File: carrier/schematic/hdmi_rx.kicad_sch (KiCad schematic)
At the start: 8 parts, among them J9001 HDMI-019S, U9001 M24C02-WMN6TP

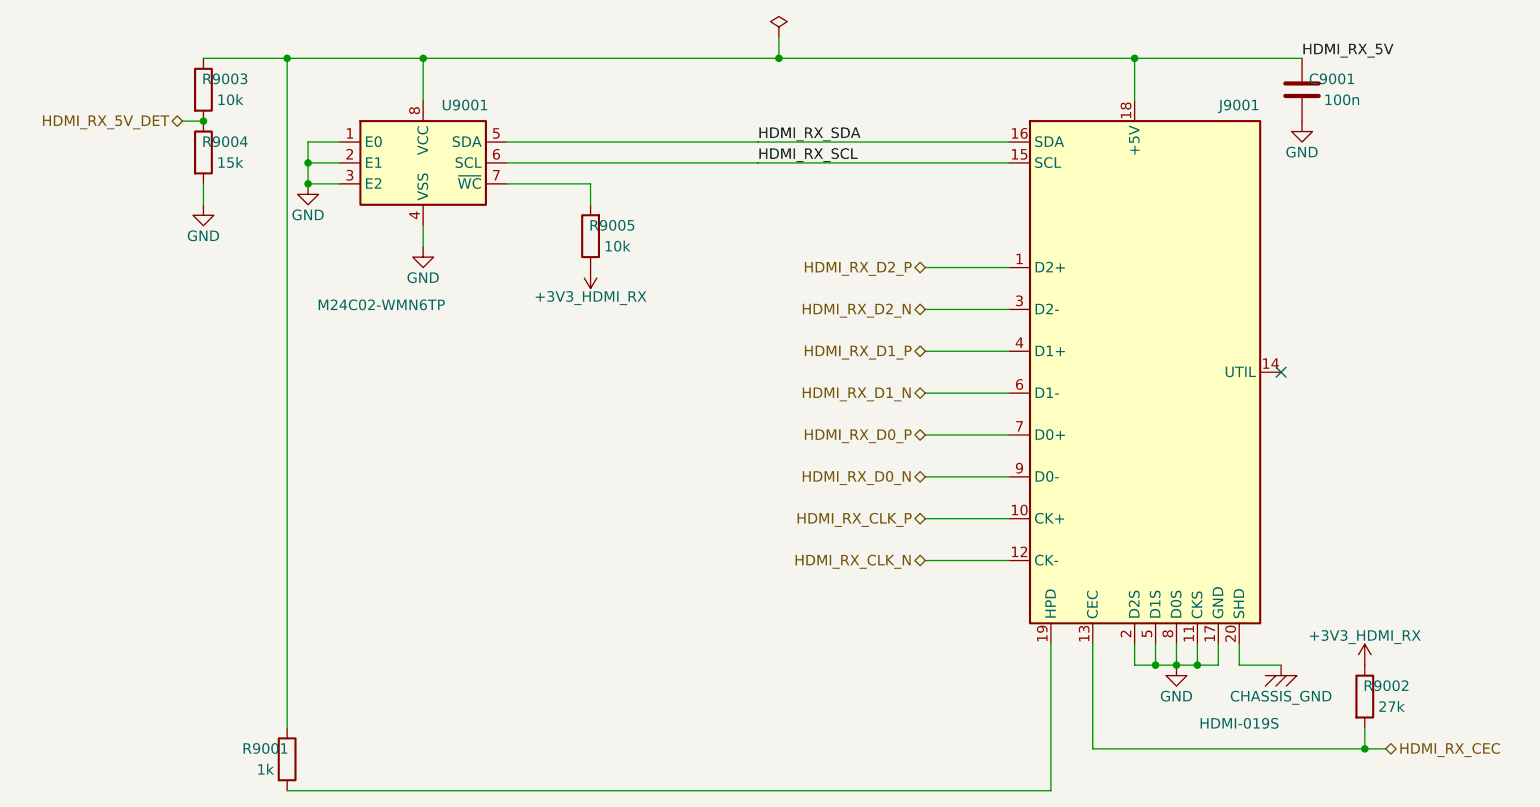
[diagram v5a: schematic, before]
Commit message: hdmi_rx COMP-1: EDID WC# hardwired to its 5V VCC (netlist FIX) + generic place.py escape-lane BFS
COMP-1 closed properly: WC# (U1.7) now on HDMI_RX_5V (the EEPROM's own VCC,
adjacent U1.8) = permanent write-protect at the right rail + above VIH whenever
the EEPROM is powered (carrier on OR off); R5 strap + HDMI_RX_EDID_WP jumper net
deleted. KiCad-extracted netlist confirms /HDMI_RX_5V = {C1,J1.18,R1,R3,U1.7,U1.8}.
The dense-sheet placement that blocked it is solved GENERICALLY in schgen/place.py:
_escape_lane tries both flanks, and direct trunk side-taps get a corner-minimizing
free-cell BFS detour (_bfs_escape, Dijkstra over (cell,heading), vertex-disjoint vs
foreign geometry — cannot short/cross). No gate softened, no sheet-specific hack.
Full regression GREEN: 25 sheets all gates, LINK 0/0, only hdmi_rx+place.py changed
(no other sheet regressed), selftest 44/44 + determinism, m1_rc PASS, render eyeballed.

Co-Authored-By: Claude Fable 5 <noreply@anthropic.com>
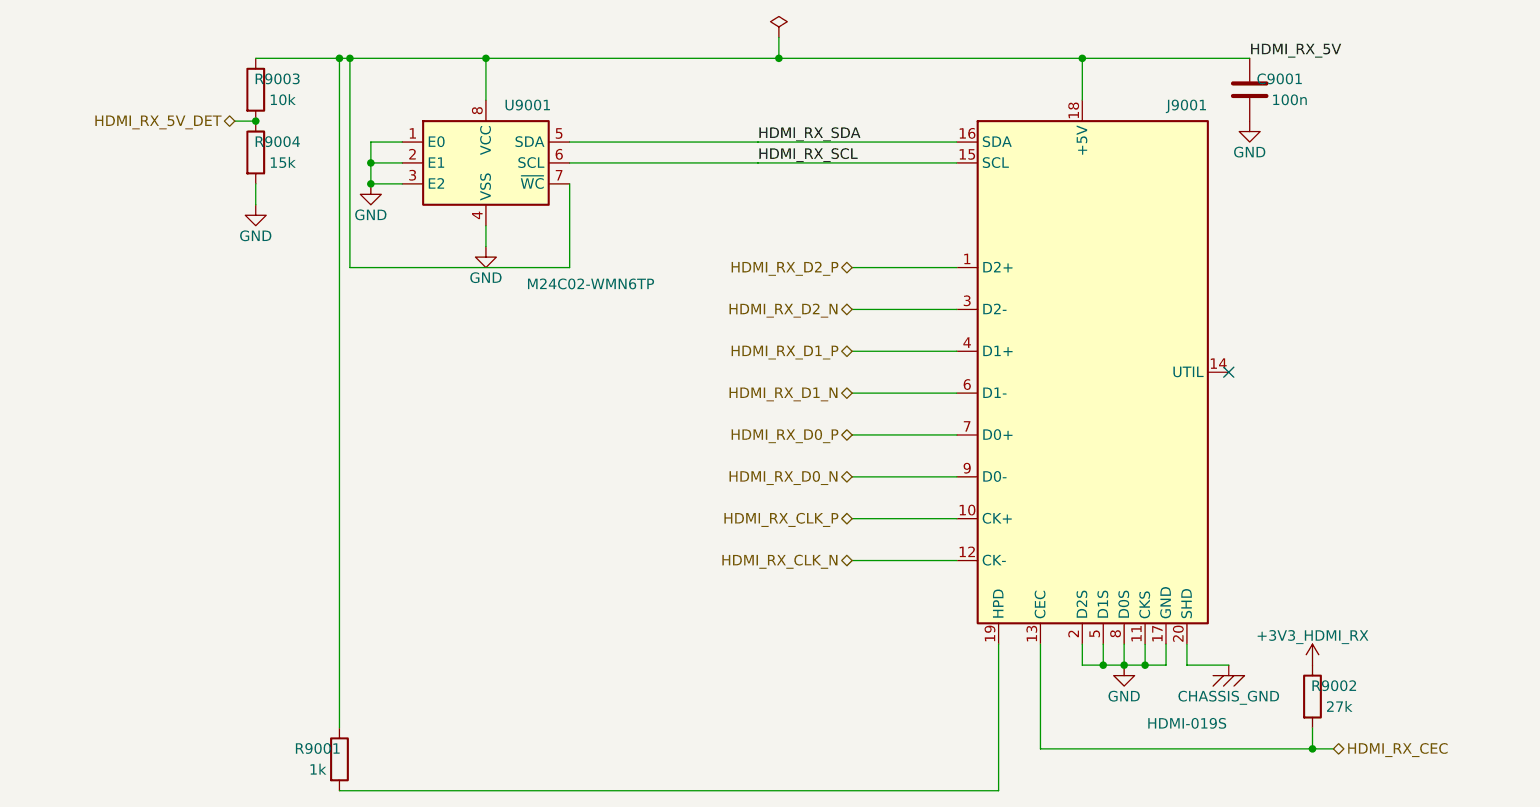
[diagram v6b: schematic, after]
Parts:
- removed C9001: 100n, Capacitor_SMD:C_0603_1608Metric, symbol Device:C
- C9001: renamed from R9004; value 15k -> 100n; footprint Resistor_SMD:R_0603_1608Metric -> Capacitor_SMD:C_0603_1608Metric; symbol Device:R -> Device:C; LCSC C22809 -> C14663
- J9001: renamed from R9005; value 10k -> HDMI-019S; footprint Resistor_SMD:R_0603_1608Metric -> HDMI-019S:HDMI-019S; symbol Device:R -> schgen:HDMI_A_RX; LCSC C25804 -> C111617; MPN (none) -> HDMI-019S
- R9001: renamed from R9002; value 27k -> 1k; LCSC C22967 -> C21190
- R9002: renamed from J9001; value HDMI-019S -> 27k; footprint HDMI-019S:HDMI-019S -> Resistor_SMD:R_0603_1608Metric; symbol schgen:HDMI_A_RX -> Device:R; LCSC C111617 -> C22967; MPN HDMI-019S -> (none)
- R9003: renamed from R9001; value 1k -> 10k; LCSC C21190 -> C25804
- R9004: renamed from R9003; value 10k -> 15k; LCSC C25804 -> C22809
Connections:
- net +3V3_HDMI_RX: now also R9002.1; no longer J9001.1, R9001.1
- net CHASSIS_GND: now also J9001.20 (SHD), J9001.21 (SHD), J9001.22 (SHD), J9001.23 (SHD); no longer R9002.20 (SHD), R9002.21 (SHD), R9002.22 (SHD), R9002.23 (SHD)
- net GND: now also J9001.11 (CKS), J9001.17 (GND), J9001.2 (D2S), J9001.5 (D1S), J9001.8 (D0S), R9004.2; no longer R9002.11 (CKS), R9002.17 (GND), R9002.2 (D2S), R9002.5 (D1S), R9002.8 (D0S)
- net HDMI_RX_5V: now also C9001.1, J9001.18 (+5V), R9001.1, U9001.7 (~{WC}); no longer R9002.18 (+5V), R9004.1
- net HDMI_RX_5V_DET: now also R9003.2, R9004.1; no longer C9001.1, R9004.2
- net HDMI_RX_CEC: now also J9001.13 (CEC), R9002.2; no longer R9001.2, R9002.13 (CEC)
- net HDMI_RX_CLK_N: now also J9001.12 (CK-); no longer R9002.12 (CK-)
- net HDMI_RX_CLK_P: now also J9001.10 (CK+); no longer R9002.10 (CK+)
- net HDMI_RX_D0_N: now also J9001.9 (D0-); no longer R9002.9 (D0-)
- net HDMI_RX_D0_P: now also J9001.7 (D0+); no longer R9002.7 (D0+)
- net HDMI_RX_D1_N: now also J9001.6 (D1-); no longer R9002.6 (D1-)
- net HDMI_RX_D1_P: now also J9001.4 (D1+); no longer R9002.4 (D1+)
- net HDMI_RX_D2_N: now also J9001.3 (D2-); no longer R9002.3 (D2-)
- net HDMI_RX_D2_P: now also J9001.1 (D2+); no longer R9002.1 (D2+)
- net HDMI_RX_SCL: now also J9001.15 (SCL); no longer R9002.15 (SCL)
- net HDMI_RX_SDA: now also J9001.16 (SDA); no longer R9002.16 (SDA)
- new net: J9001.19 (HPD), R9001.2
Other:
- moved on the sheet: R9001, R9003, R9004, U9001

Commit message: genpolish: TITLE-1 — populate the schematic title block on every sheet
Every sheet rendered a blank Title/Rev/Date — the clearest 'not a real
schematic' tell. emit() now writes a (title_block ...) after the paper node:
title = the sheet circuit's title, company "Zynq SoM Carrier", and a
"<sheet> — generated by schgen (do not hand-edit)" comment. NO date node — a
wall-clock date would break byte-determinism; the content-derived fields keep
every rebuild identical. Verified on A4 (usb_pd) and the dense A3 (power): the
block fills the standard reserved corner with zero drawing overlap. All 26
sheets, goldens re-blessed, board PASS + deterministic, selftest 53/53, m1,
pytest 147.

Co-Authored-By: Claude Opus 4.8 <noreply@anthropic.com>
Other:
- company: (none) -> Zynq SoM Carrier
- title: (none) -> HDMI RX: HDMI-A sink + EDID EEPROM
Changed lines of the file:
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@@
 	(generator_version "1.0")
 	(paper "A4")
+	(title_block
+		(title "HDMI RX: HDMI-A sink + EDID EEPROM")
+		(company "Zynq SoM Carrier")
+		(comment 1 "hdmi_rx — generated by schgen (do not hand-edit)")
+	)
 	(wire
 		(pts

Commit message: board: four board-management HW blocks on a manually-gated +3V3_AUX (BOARDHW)
The four services the carrier was missing — all behind ONE manual power enable
(C1) on two new sheets split so neither defeats the placer's rail-stub router:

  board_aux       — the gate + I2C isolator (infrastructure)
  board_services  — ID-EEPROM + RTC + watchdog + QWIIC (the peripherals)

WHAT LANDED
  * 24AA025E48 (C129895)  ID-EEPROM with a factory EUI-48 **MAC** for the
      LAN8720/RJ45 — strapped 0x51 (0x50 is the FMC EEPROM).
  * RV-3028-C7 (C3019759) I2C RTC, integrated DTCXO (no crystal), CR1220 coin
      cell (KH-CR1220-2) with auto-switchover, 0x52.
  * TPS3823-33 (C7719)    supervisor + windowed watchdog.
  * ZX-SH1.0-4PWT (C7430446)  QWIIC / STEMMA-QT expansion (gated 3V3 + the
      isolated AUX I2C).
  * SY6280 gate + DSHP04 DIP + PCA9306 isolator complete the infrastructure.

CONSTRAINTS (the user's three standing requirements)
  C1 manual enable "like the previous": +3V3_AUX is a SY6280 load switch whose
     EN is a default-OFF DSHP04 DIP (100k pulldown) — the same gated-module
     idiom, self-contained so it touches none of the dense rail/EN sheets.
  C2 "no watchdog reset during power-up": THREE independent guards — (1) the
     supervisor's VDD is the default-OFF +3V3_AUX, so it is UNPOWERED through
     power-up; (2) the TPS3823 disables its watchdog while WDI floats, and WDI
     is driven only by the PL (WATCHDOG_KICK, Hi-Z until the fabric is up); (3)
     RESET# is a firmware-mediated PL EVENT (J3.31), never a rail/POR line.
  C3 Zynq-agnostic: the only SoM-side signals (the 2 watchdog lines) ride PL
     bank-35 IO by their contract net names (IO_L16_N/P_35 -> J3.29/31); xdc.py
     emits the constraints live — nothing hard-codes the Zynq part.

LAW 0 (electrical integrity): the peripherals sit on the GATED rail but their
bus is the always-on STM32_I2C2 management bus. A PCA9306 bridges them with EN
tied to +3V3_AUX, so the switch OPENS whenever the rail is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
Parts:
- renumbered C9001 to C11001, J9001 to J11001, R9001 to R11001, R9002 to R11002, R9003 to R11003, R9004 to R11004, U9001 to U11001
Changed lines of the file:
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@@
 		(property
 			"Reference"
-			"U9001"
+			"U11001"
 			(at 119.38 57.785 0)
 			(effects
@@
 				(path
 					"/c2797150-7a6e-556a-82f5-fdda13c31368/1e15c56c-3a37-58d2-aa9b-64efface14d2"
-					(reference "U9001")
+					(reference "U11001")
 					(unit 1)
 				)
@@
 		(property
 			"Reference"
-			"J9001"
+			"J11001"
 			(at 199.39 57.785 0)
 			(effects
@@
 				(path
 					"/c2797150-7a6e-556a-82f5-fdda13c31368/1e15c56c-3a37-58d2-aa9b-64efface14d2"
-					(reference "J9001")
+					(reference "J11001")
 					(unit 1)
 				)
@@
 		(property
 			"Reference"
-			"R9002"
+			"R11002"
 			(at 217.273 128.27 0)
 			(effects
@@
 				(path
 					"/c2797150-7a6e-556a-82f5-fdda13c31368/1e15c56c-3a37-58d2-aa9b-64efface14d2"
-					(reference "R9002")
+					(reference "R11002")
 					(unit 1)
 				)
@@
 		(property
 			"Reference"
-			"R9001"
+			"R11001"
 			(at 93.877 135.89 0)
 			(effects
@@
 				(path
 					"/c2797150-7a6e-556a-82f5-fdda13c31368/1e15c56c-3a37-58d2-aa9b-64efface14d2"
-					(reference "R9001")
+					(reference "R11001")
 					(unit 1)
 				)
@@
 		(property
 			"Reference"
-			"R9003"
+			"R11003"
 			(at 89.002 54.61 0)
 			(effects
@@
 				(path
 					"/c2797150-7a6e-556a-82f5-fdda13c31368/1e15c56c-3a37-58d2-aa9b-64efface14d2"
-					(reference "R9003")
+					(reference "R11003")
 					(unit 1)
 				)
@@
 		(property
 			"Reference"
-			"R9004"
+			"R11004"
 			(at 89.002 62.23 0)
 			(effects
@@
 				(path
 					"/c2797150-7a6e-556a-82f5-fdda13c31368/1e15c56c-3a37-58d2-aa9b-64efface14d2"
-					(reference "R9004")
+					(reference "R11004")
 					(unit 1)
 				)
@@
 		(property
 			"Reference"
-			"C9001"
+			"C11001"
 			(at 210.668 54.61 0)
 			(effects
@@
 				(path
 					"/c2797150-7a6e-556a-82f5-fdda13c31368/1e15c56c-3a37-58d2-aa9b-64efface14d2"
-					(reference "C9001")
+					(reference "C11001")
 					(unit 1)
 				)
@@
 		(property
 			"Reference"
-			"#PWR9001"
+			"#PWR11001"
 			(at 100.33 64.77 0)
 			(effects
@@
 				(path
 					"/c2797150-7a6e-556a-82f5-fdda13c31368/1e15c56c-3a37-58d2-aa9b-64efface14d2"
-					(reference "#PWR9001")
+					(reference "#PWR11001")
 					(unit 1)
 				)
@@
 		(property
 			"Reference"
-			"#PWR9002"
+			"#PWR11002"
 			(at 114.3 72.39 0)
 			(effects
@@
 				(path
 					"/c2797150-7a6e-556a-82f5-fdda13c31368/1e15c56c-3a37-58d2-aa9b-64efface14d2"
-					(reference "#PWR9002")
+					(reference "#PWR11002")
 					(unit 1)
 				)
@@
 		(property
 			"Reference"
-			"#PWR9003"
+			"#PWR11003"
 			(at 191.77 123.19 0)
 			(effects
@@
 				(path
 					"/c2797150-7a6e-556a-82f5-fdda13c31368/1e15c56c-3a37-58d2-aa9b-64efface14d2"
-					(reference "#PWR9003")
+					(reference "#PWR11003")
 					(unit 1)
 				)
@@
 		(property
 			"Reference"
-			"#PWR9004"
+			"#PWR11004"
 			(at 204.47 123.19 0)
 			(effects
@@
 				(path
 					"/c2797150-7a6e-556a-82f5-fdda13c31368/1e15c56c-3a37-58d2-aa9b-64efface14d2"
-					(reference "#PWR9004")
+					(reference "#PWR11004")
 					(unit 1)
 				)
@@
 		(property
 			"Reference"
-			"#PWR9005"
+			"#PWR11005"
 			(at 214.63 123.19 0)
 			(effects
@@
 				(path
 					"/c2797150-7a6e-556a-82f5-fdda13c31368/1e15c56c-3a37-58d2-aa9b-64efface14d2"
-					(reference "#PWR9005")
+					(reference "#PWR11005")
 					(unit 1)
 				)
@@
 		(property
 			"Reference"
-			"#PWR9006"
+			"#PWR11006"
 			(at 86.36 67.31 0)
 			(effects
@@
 				(path
 					"/c2797150-7a6e-556a-82f5-fdda13c31368/1e15c56c-3a37-58d2-aa9b-64efface14d2"
-					(reference "#PWR9006")
+					(reference "#PWR11006")
 					(unit 1)
 				)
@@
 		(property
 			"Reference"
-			"#PWR9007"
+			"#PWR11007"
 			(at 207.01 57.15 0)
 			(effects
@@
 				(path
 					"/c2797150-7a6e-556a-82f5-fdda13c31368/1e15c56c-3a37-58d2-aa9b-64efface14d2"
-					(reference "#PWR9007")
+					(reference "#PWR11007")
 					(unit 1)
 				)
@@
 		(property
 			"Reference"
-			"#FLG9001"
+			"#FLG11001"
 			(at 149.86 46.99 0)
 			(effects
@@
 				(path
 					"/c2797150-7a6e-556a-82f5-fdda13c31368/1e15c56c-3a37-58d2-aa9b-64efface14d2"
-					(reference "#FLG9001")
-					(unit 1)
-				)
+					(reference "#FLG11001")
+					(unit 1)
+				)
